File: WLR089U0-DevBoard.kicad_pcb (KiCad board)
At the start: 2 copper layers, 0 parts

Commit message: pcb making started
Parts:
- added C1: 1u, Capacitor_SMD:C_1206_3216Metric_Pad1.33x1.80mm_HandSolder, F.Cu at (126.3, 83.4)
- added C2: 1u, Capacitor_SMD:C_1206_3216Metric_Pad1.33x1.80mm_HandSolder, F.Cu at (126.0, 86.8)
- added C3: 100n, Capacitor_SMD:C_1206_3216Metric_Pad1.33x1.80mm_HandSolder, F.Cu at (148.5, 83.3)
- added D1: Red, LED_SMD:LED_0805_2012Metric_Pad1.15x1.40mm_HandSolder, F.Cu at (135.0, 83.5)
- added D2: Green, LED_SMD:LED_0805_2012Metric_Pad1.15x1.40mm_HandSolder, F.Cu at (127.7, 90.8)
- added IC1: WLR089U0-I_RM, SamacSys_Parts:WLR089U0IRM, F.Cu at (136.4, 105.7)
- added J1: USB_B_Micro, Connector_USB:USB_Micro-AB_Molex_47590-0001, F.Cu at (137.0, 77.1)
- added J2: Conn_ARM_JTAG_SWD_10, Connector_PinHeader_1.27mm:PinHeader_2x05_P1.27mm_Vertical, F.Cu at (136.9, 93.2)
- added J3: Conn_01x10_Female, Connector_PinHeader_2.54mm:PinHeader_1x10_P2.54mm_Vertical, F.Cu at (124.2, 93.7)
- added J4: Conn_01x10_Male, Connector_PinHeader_2.54mm:PinHeader_1x10_P2.54mm_Vertical, F.Cu at (124.5, 120.4)
- added J5: Conn_01x10_Female, Connector_PinHeader_2.54mm:PinHeader_1x10_P2.54mm_Vertical, F.Cu at (148.4, 116.6)
- added J6: Conn_01x02_Male, Connector_PinHeader_2.54mm:PinHeader_1x02_P2.54mm_Vertical, F.Cu at (144.1, 78.1)
- added JP1: SolderJumper_3_Bridged12, Jumper:SolderJumper-3_P1.3mm_Bridged12_RoundedPad1.0x1.5mm_NumberLabels, F.Cu at (142.7, 88.3)
- added JP2: SolderJumper_3_Bridged12, Jumper:SolderJumper-3_P1.3mm_Bridged12_RoundedPad1.0x1.5mm_NumberLabels, F.Cu at (137.6, 88.2)
- added JP3: SolderJumper_2_Open, Jumper:SolderJumper-3_P1.3mm_Open_RoundedPad1.0x1.5mm, F.Cu at (145.2, 83.9)
- added R1: 100k, Resistor_SMD:R_1206_3216Metric_Pad1.42x1.75mm_HandSolder, F.Cu at (148.2, 87.5)
- added R2: 1k, Resistor_SMD:R_1206_3216Metric_Pad1.42x1.75mm_HandSolder, F.Cu at (131.6, 87.2)
- added R3: 1k, Resistor_SMD:R_1206_3216Metric_Pad1.42x1.75mm_HandSolder, F.Cu at (132.3, 90.7)
- added SW1: SW_Push, WLR089u0-DevBoard:Tactile Switch 3x4x2mm, F.Cu at (146.8, 88.2)
- added TP1: TestPoint, MountingHole:MountingHole_2.2mm_M2_DIN965_Pad_TopBottom, F.Cu at (129.1, 77.4)
- added TP2: TestPoint, MountingHole:MountingHole_2.2mm_M2_DIN965_Pad_TopBottom, F.Cu at (150.8, 78.2)
- added TP3: TestPoint, MountingHole:MountingHole_2.2mm_M2_DIN965_Pad_TopBottom, F.Cu at (124.7, 77.4)
- added U1: MCP1700-3302E_SOT23, Package_TO_SOT_SMD:SOT-23, F.Cu at (130.9, 83.2)
- added U2: CH304E, Package_SO:MSOP-10_3x3mm_P0.5mm, F.Cu at (139.6, 83.7)
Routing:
- net Net-(JP2-Pad1): track 0.00 -> 1.80 mm
- net GND: track 0.00 -> 0.50 mm
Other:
- board outline added: 7.5 x 2 mm

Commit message: pcb editing
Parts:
- moved J2 29.1 mm to (109.4, 83.8)
- moved JP1 21.8 mm to (121.4, 83.4), turned to 270 degrees
- moved SW1 19.8 mm to (127.0, 87.9)
- moved JP3 16.8 mm to (128.8, 87.1), turned to 0 degrees
- moved TP2 15.9 mm to (135.0, 77.4)
- moved J6 15.2 mm to (128.9, 77.1)
- moved J1 14.6 mm to (122.4, 77.2)
- moved R1 14.4 mm to (133.8, 87.2)
- moved C3 14.4 mm to (134.2, 83.1)
- moved C1 14.0 mm to (112.9, 87.2)
- moved JP2 14.0 mm to (123.7, 87.1)
- moved J3 13.9 mm to (110.6, 90.5)
- moved J4 13.9 mm to (110.9, 117.2)
- moved IC1 13.9 mm to (122.9, 102.6)
- moved J5 13.9 mm to (134.9, 113.4)
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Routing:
- net Net-(JP2-Pad1): track 1.80 -> 0.85 mm
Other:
- outline, holes or cut-outs redrawn

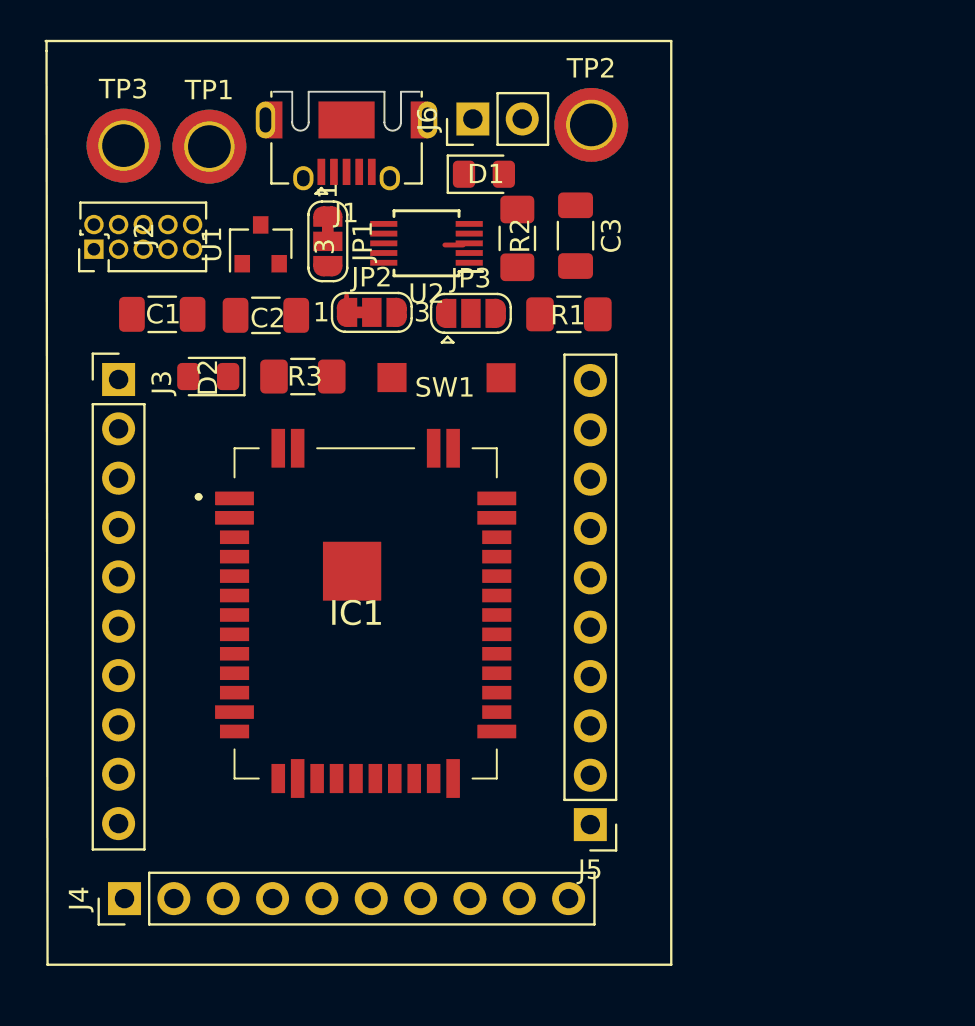
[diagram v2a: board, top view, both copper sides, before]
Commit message: removed 5v test point, edited layout edge,microusb edge
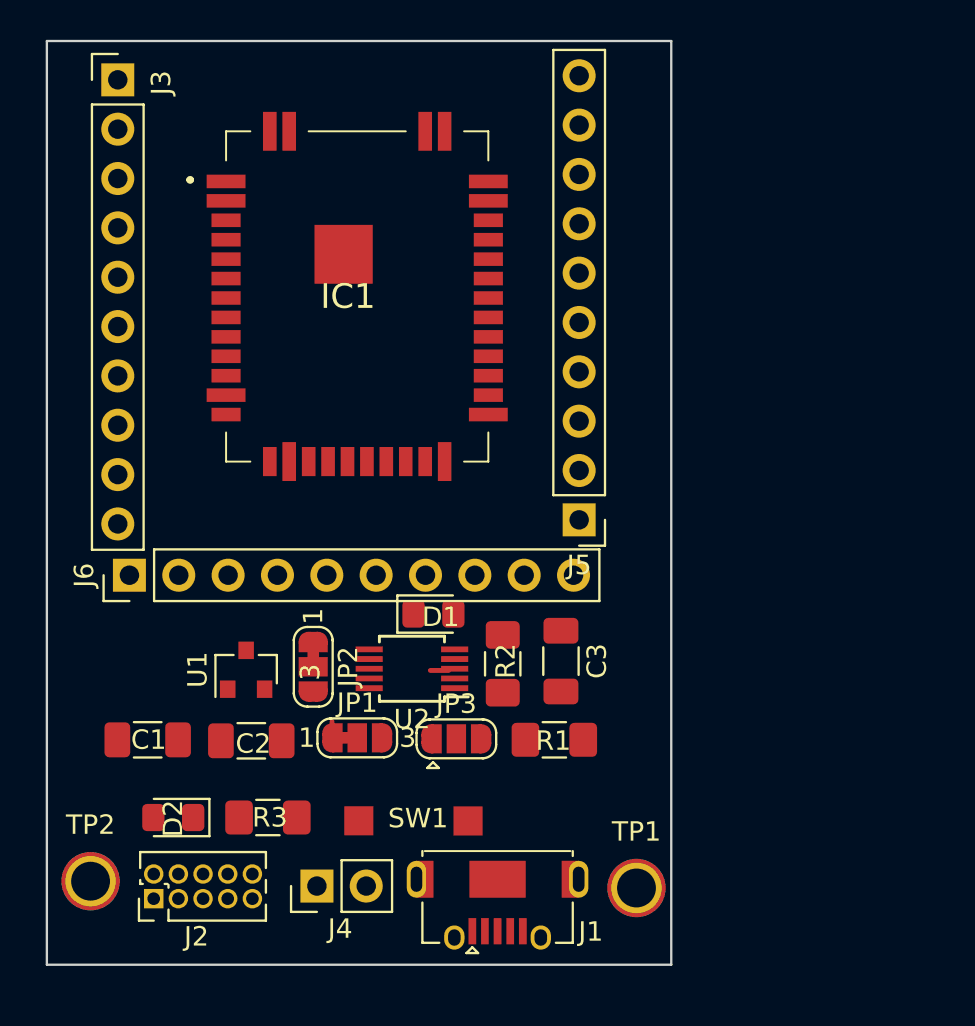
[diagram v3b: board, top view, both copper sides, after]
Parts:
- removed the TP1 at (115.3, 78.5)
- moved J4 40.3 mm to (120.8, 116.6)
- moved J1 39.9 mm to (130.2, 116.2)
- moved TP1 39.3 mm to (137.3, 116.7)
- moved TP2 37.9 mm to (109.2, 116.3)
- moved J2 33.6 mm to (112.5, 117.2)
- moved SW1 22.9 mm to (125.3, 110.7)
- moved D1 22.8 mm to (126.8, 102.6)
- moved D2 22.8 mm to (113.5, 113.1)
- moved R3 22.8 mm to (118.3, 113.1)
- moved C1 21.9 mm to (112.1, 109.1)
- moved C3 21.9 mm to (133.4, 105.0)
- moved JP3 21.9 mm to (128.0, 109.0)
- moved R1 21.9 mm to (133.1, 109.1)
- moved U2 21.9 mm to (125.7, 105.4)
- moved C2 21.9 mm to (117.5, 109.1)
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- renumbered J6 to J4, J4 to J6, JP2 to JP1, JP1 to JP2, TP2 to TP1, TP3 to TP2
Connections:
- J2 pad 6: Net-(J2-Pad6) -> (no net)
- J2 pad 7: Net-(J2-Pad7) -> (no net)
- J2 pad 8: Net-(J2-Pad8) -> (no net)
- U2 pad 4: Net-(U2-Pad4) -> (no net)
- U2 pad 5: Net-(U2-Pad5) -> (no net)
- U2 pad 6: Net-(U2-Pad6) -> (no net)
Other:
- board size 7.5 x 2 mm -> 32.1 x 47.5 mm

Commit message: placement of ic2 done
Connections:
- J2 pad 6: (no net) -> Net-(J2-Pad6)
- J2 pad 7: (no net) -> Net-(J2-Pad7)
- J2 pad 8: (no net) -> Net-(J2-Pad8)
- J3 pad 5: PA18 -> S1_I2C_SDA
- J3 pad 6: PA19 -> S1_I2C_SCL
- J3 pad 7: PA15 -> PA18
- J3 pad 8: PA14 -> PA19
- J3 pad 9: GND -> PA15
- J5 pad 2: PA22 -> GND
- J6 pad 3: S1_I2C_SCL -> PA14
- J6 pad 4: S1_I2C_SDA -> S5_MOSI
- J6 pad 5: S5_MOSI -> S5_SS
- J6 pad 6: S5_SS -> S5_SCK
- J6 pad 7: S5_SCK -> S5_MISO
- J6 pad 8: S5_MISO -> PA22
- U2 pad 4: (no net) -> Net-(U2-Pad4)
- U2 pad 5: (no net) -> Net-(U2-Pad5)
- U2 pad 6: (no net) -> Net-(U2-Pad6)
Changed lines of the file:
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@@
-(kicad_pcb (version 20171130) (host pcbnew "(5.1.8)-1")
+(kicad_pcb (version 20171130) (host pcbnew "(5.1.4)-1")
   (general
     (thickness 1.6)
@@
     (zones 0)
     (modules 23)
-    (nets 38)
+    (nets 44)
   )
   (page A4)
@@
   (net 36 "Net-(JP1-Pad1)")
   (net 37 "Net-(JP2-Pad1)")
+  (net 38 "Net-(J2-Pad6)")
+  (net 39 "Net-(J2-Pad7)")
+  (net 40 "Net-(J2-Pad8)")
+  (net 41 "Net-(U2-Pad4)")
+  (net 42 "Net-(U2-Pad5)")
+  (net 43 "Net-(U2-Pad6)")
   (net_class Default "This is the default net class."
     (clearance 0.2)
@@
     (pad 5 thru_hole oval (at 0 2.54 90) (size 1 1) (drill 0.65) (layers *.Cu *.Mask)
       (net 2 GND))
-    (pad 6 thru_hole oval (at 1.27 2.54 90) (size 1 1) (drill 0.65) (layers *.Cu *.Mask))
-    (pad 7 thru_hole oval (at 0 3.81 90) (size 1 1) (drill 0.65) (layers *.Cu *.Mask))
-    (pad 8 thru_hole oval (at 1.27 3.81 90) (size 1 1) (drill 0.65) (layers *.Cu *.Mask))
+    (pad 6 thru_hole oval (at 1.27 2.54 90) (size 1 1) (drill 0.65) (layers *.Cu *.Mask)
+      (net 38 "Net-(J2-Pad6)"))
+    (pad 7 thru_hole oval (at 0 3.81 90) (size 1 1) (drill 0.65) (layers *.Cu *.Mask)
+      (net 39 "Net-(J2-Pad7)"))
+    (pad 8 thru_hole oval (at 1.27 3.81 90) (size 1 1) (drill 0.65) (layers *.Cu *.Mask)
+      (net 40 "Net-(J2-Pad8)"))
     (pad 9 thru_hole oval (at 0 5.08 90) (size 1 1) (drill 0.65) (layers *.Cu *.Mask)
       (net 2 GND))
@@
       (net 2 GND))
     (pad 9 thru_hole oval (at 0 20.32) (size 1.7 1.7) (drill 1) (layers *.Cu *.Mask)
-      (net 2 GND))
+      (net 15 PA15))
     (pad 8 thru_hole oval (at 0 17.78) (size 1.7 1.7) (drill 1) (layers *.Cu *.Mask)
-      (net 16 PA14))
+      (net 14 PA19))
     (pad 7 thru_hole oval (at 0 15.24) (size 1.7 1.7) (drill 1) (layers *.Cu *.Mask)
-      (net 15 PA15))
+      (net 13 PA18))
     (pad 6 thru_hole oval (at 0 12.7) (size 1.7 1.7) (drill 1) (layers *.Cu *.Mask)
-      (net 14 PA19))
+      (net 12 S1_I2C_SCL))
     (pad 5 thru_hole oval (at 0 10.16) (size 1.7 1.7) (drill 1) (layers *.Cu *.Mask)
-      (net 13 PA18))
+      (net 11 S1_I2C_SDA))
     (pad 4 thru_hole oval (at 0 7.62) (size 1.7 1.7) (drill 1) (layers *.Cu *.Mask)
       (net 10 PA27))
@@
       (net 2 GND))
     (pad 3 thru_hole oval (at 0 5.08 90) (size 1.7 1.7) (drill 1) (layers *.Cu *.Mask)
-      (net 12 S1_I2C_SCL))
+      (net 16 PA14))
     (pad 4 thru_hole oval (at 0 7.62 90) (size 1.7 1.7) (drill 1) (layers *.Cu *.Mask)
-      (net 11 S1_I2C_SDA))
+      (net 17 S5_MOSI))
     (pad 5 thru_hole oval (at 0 10.16 90) (size 1.7 1.7) (drill 1) (layers *.Cu *.Mask)
-      (net 17 S5_MOSI))
+      (net 18 S5_SS))
     (pad 6 thru_hole oval (at 0 12.7 90) (size 1.7 1.7) (drill 1) (layers *.Cu *.Mask)
-      (net 18 S5_SS))
+      (net 19 S5_SCK))
     (pad 7 thru_hole oval (at 0 15.24 90) (size 1.7 1.7) (drill 1) (layers *.Cu *.Mask)
-      (net 19 S5_SCK))
+      (net 20 S5_MISO))
     (pad 8 thru_hole oval (at 0 17.78 90) (size 1.7 1.7) (drill 1) (layers *.Cu *.Mask)
-      (net 20 S5_MISO))
+      (net 21 PA22))
     (pad 9 thru_hole oval (at 0 20.32 90) (size 1.7 1.7) (drill 1) (layers *.Cu *.Mask)
       (net 2 GND))
@@
       (net 25 VSW))
     (pad 2 thru_hole oval (at 0 2.54 180) (size 1.7 1.7) (drill 1) (layers *.Cu *.Mask)
-      (net 21 PA22))
+      (net 2 GND))
     (pad 1 thru_hole rect (at 0 0 180) (size 1.7 1.7) (drill 1) (layers *.Cu *.Mask)
       (net 2 GND))
@@
     (pad 3 smd rect (at -2.2 0 180) (size 1.4 0.3) (layers F.Cu F.Paste F.Mask)
       (net 2 GND))
-    (pad 4 smd rect (at -2.2 0.5 180) (size 1.4 0.3) (layers F.Cu F.Paste F.Mask))
-    (pad 5 smd rect (at -2.2 1 180) (size 1.4 0.3) (layers F.Cu F.Paste F.Mask))
-    (pad 6 smd rect (at 2.2 1 180) (size 1.4 0.3) (layers F.Cu F.Paste F.Mask))
+    (pad 4 smd rect (at -2.2 0.5 180) (size 1.4 0.3) (layers F.Cu F.Paste F.Mask)
+      (net 41 "Net-(U2-Pad4)"))
+    (pad 5 smd rect (at -2.2 1 180) (size 1.4 0.3) (layers F.Cu F.Paste F.Mask)
+      (net 42 "Net-(U2-Pad5)"))
+    (pad 6 smd rect (at 2.2 1 180) (size 1.4 0.3) (layers F.Cu F.Paste F.Mask)
+      (net 43 "Net-(U2-Pad6)"))
     (pad 7 smd rect (at 2.2 0.5 180) (size 1.4 0.3) (layers F.Cu F.Paste F.Mask)
       (net 4 "Net-(C3-Pad1)"))

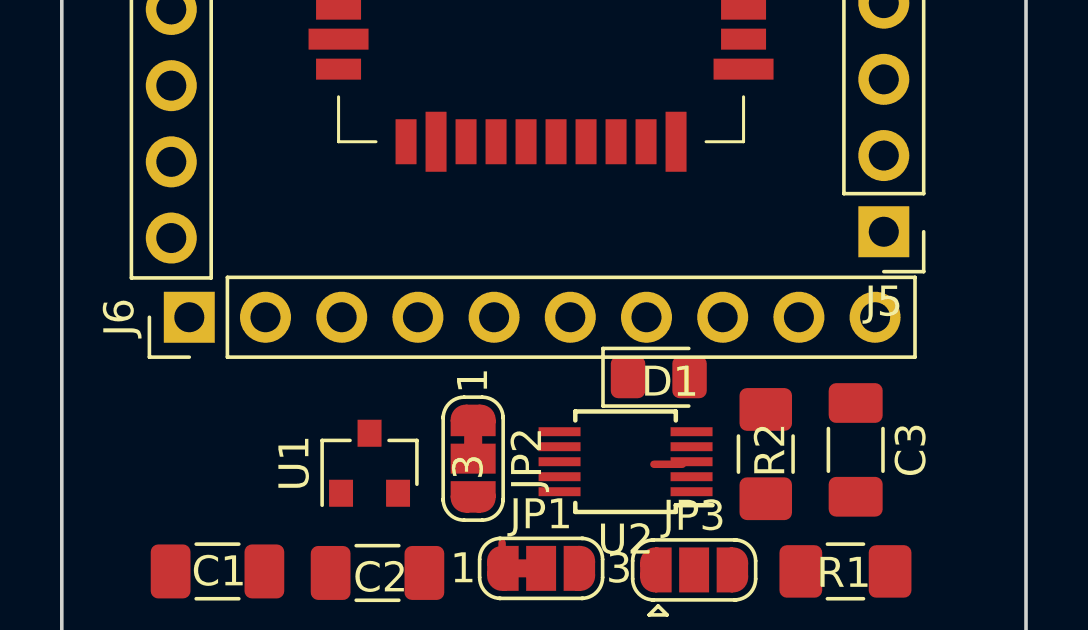
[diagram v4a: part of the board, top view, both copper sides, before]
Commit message: updated pin header to 8 pin, updated layout
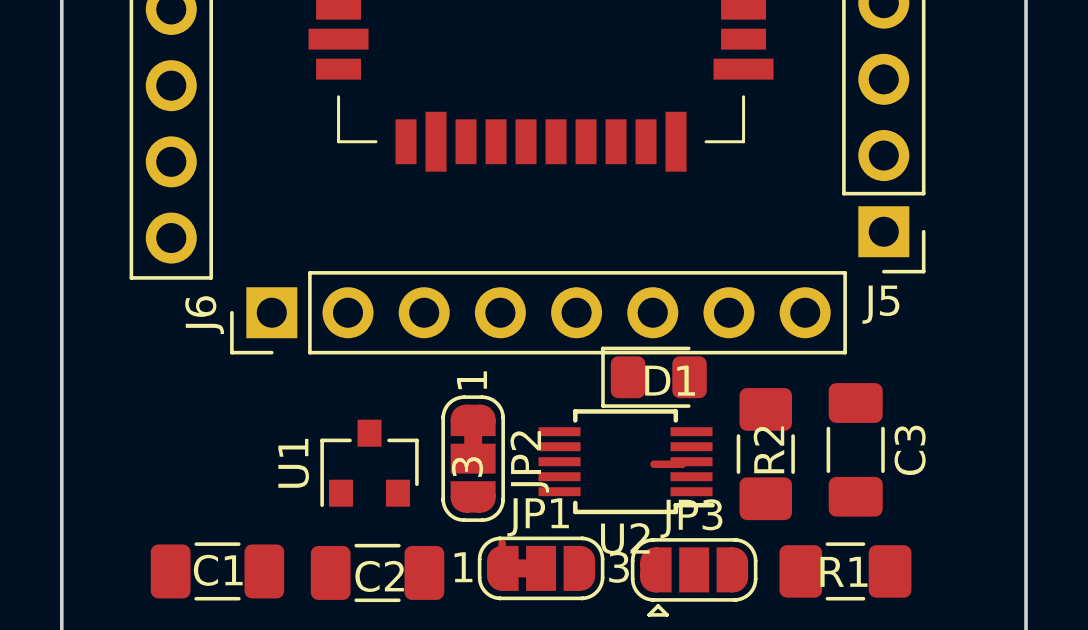
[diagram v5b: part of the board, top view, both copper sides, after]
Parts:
- J6: value Conn_01x10_Male -> Conn_01x08_Male; footprint Connector_PinHeader_2.54mm:PinHeader_1x10_P2.54mm_Vertical -> Connector_PinHeader_2.54mm:PinHeader_1x08_P2.54mm_Vertical
- moved J6 2.75 mm to (114.0, 100.5)
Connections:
- J2 pad 6: Net-(J2-Pad6) -> (no net)
- J2 pad 7: Net-(J2-Pad7) -> (no net)
- J2 pad 8: Net-(J2-Pad8) -> (no net)
- J6 pad 2: GND -> PA14
- J6 pad 3: PA14 -> S5_MOSI
- J6 pad 4: S5_MOSI -> S5_SS
- J6 pad 5: S5_SS -> S5_SCK
- J6 pad 6: S5_SCK -> S5_MISO
- J6 pad 7: S5_MISO -> PA22
- J6 pad 8: PA22 -> +3V3
- U2 pad 4: Net-(U2-Pad4) -> (no net)
- U2 pad 5: Net-(U2-Pad5) -> (no net)
- U2 pad 6: Net-(U2-Pad6) -> (no net)

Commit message: final pcb layout routing pending
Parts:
- moved R3 38.2 mm to (117.0, 74.9), turned to 180 degrees
- moved D2 37.3 mm to (113.3, 75.8), turned to 270 degrees
- moved C1 21.8 mm to (133.9, 107.7), turned to 270 degrees
- moved C3 14.7 mm to (119.2, 109.0), turned to 0 degrees
- moved JP1 14.2 mm to (109.4, 104.9), turned to 90 degrees
- moved JP3 14.1 mm to (113.9, 109.0)
- moved U1 13.0 mm to (130.0, 108.1), turned to 270 degrees
- moved U2 11.8 mm to (114.0, 105.0)
- moved SW1 11.0 mm to (135.5, 106.6), turned to 180 degrees
- moved C2 7.66 mm to (123.2, 104.1)
- moved R2 6.92 mm to (124.0, 107.6), turned to 270 degrees
- moved R1 6.73 mm to (128.6, 104.0), turned to 0 degrees
- moved D1 5.46 mm to (126.6, 108.1), turned to 270 degrees
- moved J1 4.42 mm to (130.2, 111.8)
- moved J2 4.42 mm to (112.5, 112.8)
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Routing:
- net GND: track 0.95 -> 0.00 mm
- net Net-(JP1-Pad1): track 0.85 -> 0.00 mm
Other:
- board size 32.1 x 47.5 mm -> 32.2 x 43.1 mm

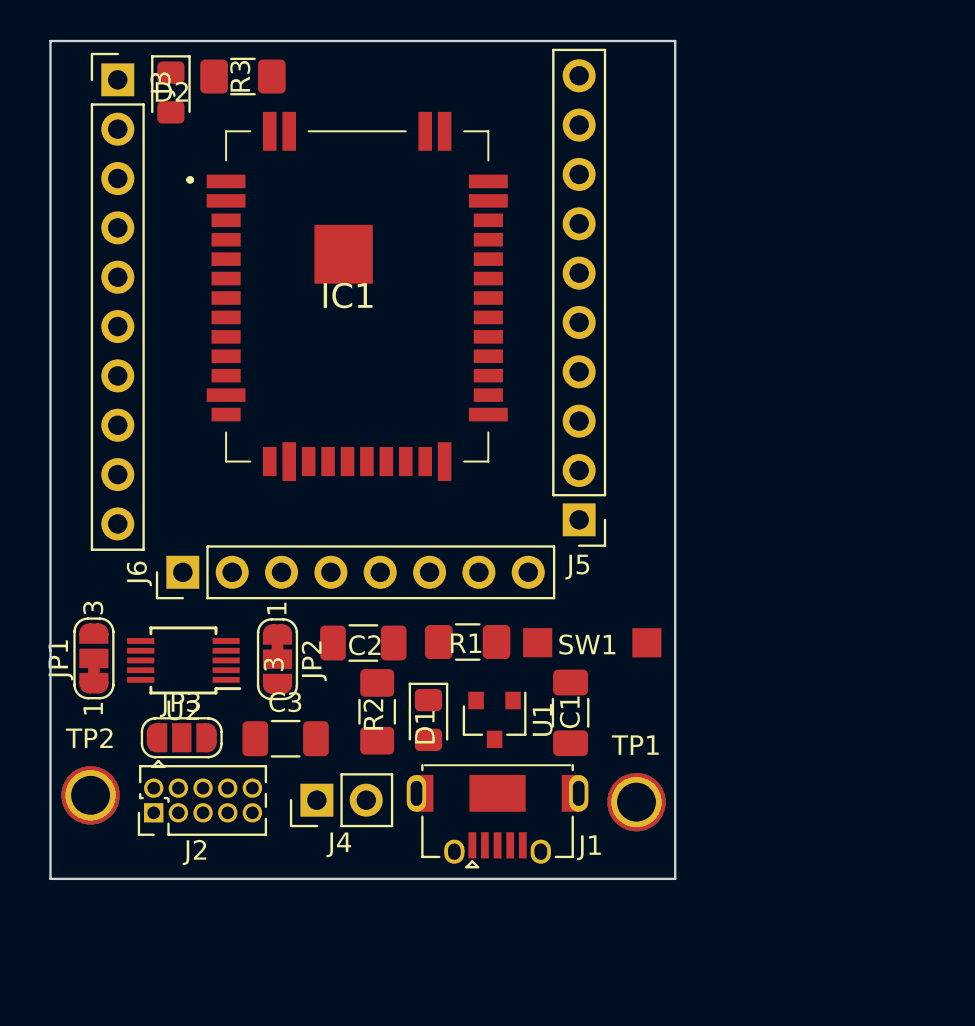
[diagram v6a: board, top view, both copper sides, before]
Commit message: rearranged layout a bit
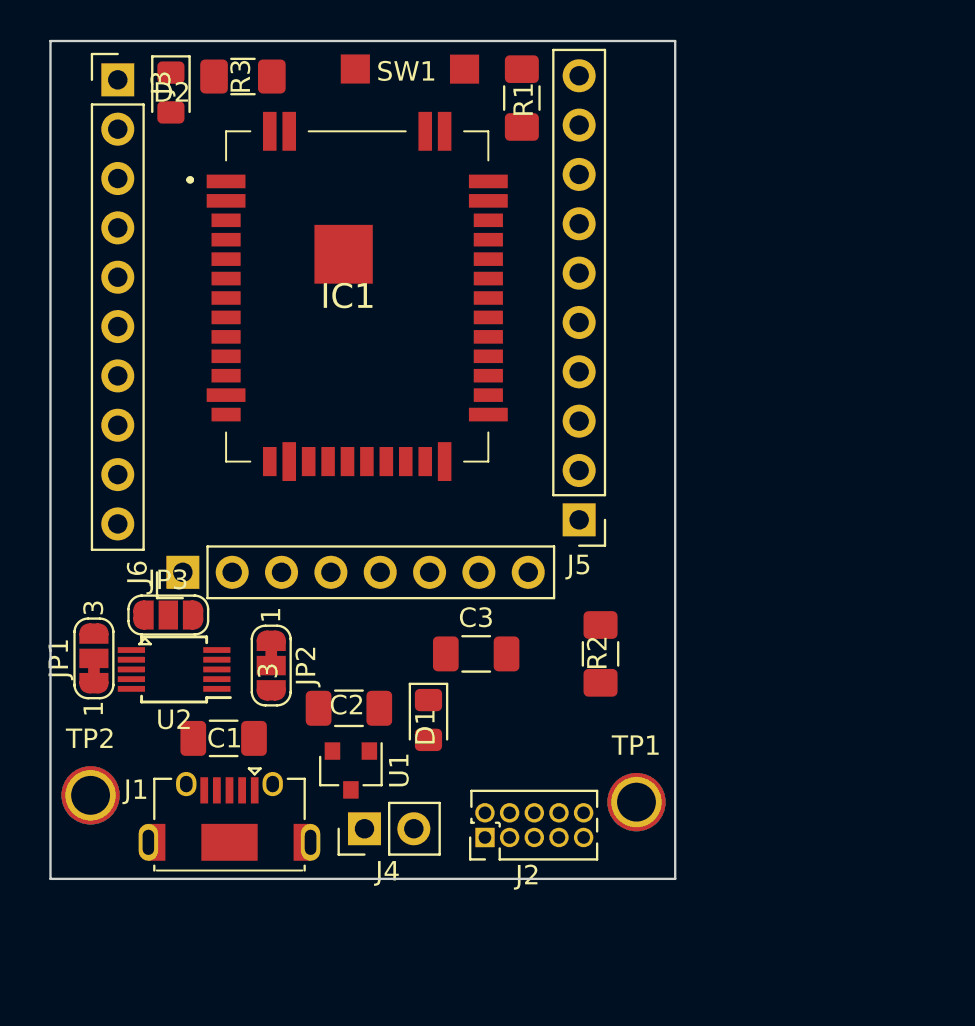
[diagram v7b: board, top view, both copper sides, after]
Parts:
- moved SW1 31.0 mm to (126.2, 77.1)
- moved R1 28.1 mm to (131.4, 76.0), turned to 90 degrees
- moved C1 17.9 mm to (116.0, 109.0), turned to 180 degrees
- moved J2 17.1 mm to (129.5, 114.1)
- moved J1 14.0 mm to (116.3, 114.3), turned to 0 degrees
- moved R2 11.9 mm to (135.4, 104.7)
- moved C3 10.7 mm to (129.1, 104.7)
- moved U1 7.84 mm to (122.6, 110.7)
- moved JP3 6.35 mm to (113.2, 102.7)
- moved C2 3.44 mm to (122.5, 107.5), turned to 0 degrees
- moved J4 2.86 mm to (123.3, 113.7)
- moved U2 0.67 mm to (113.5, 105.5)
- moved JP2 0.46 mm to (118.5, 105.2)
